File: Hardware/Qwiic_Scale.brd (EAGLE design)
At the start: 25.4 x 35.6 mm, 68 parts, among them J1 CAP, J2 Qwiic, J3 PTH, J4 Qwiic, J7 Spring Terminal, U1 NAU7802

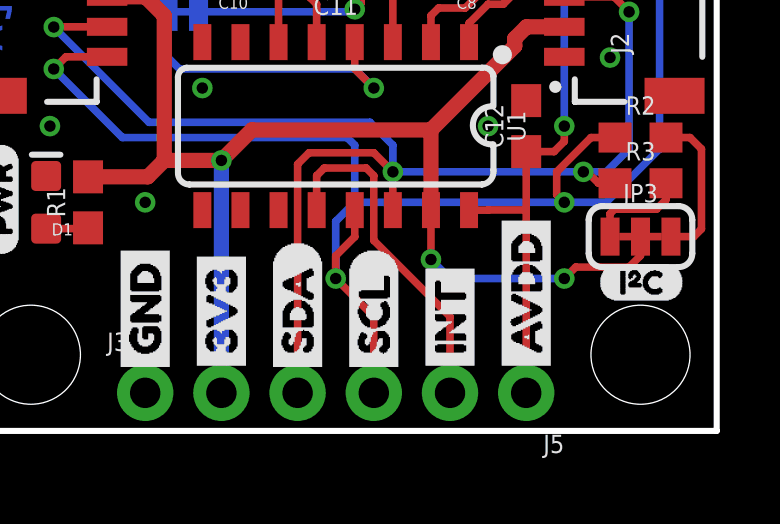
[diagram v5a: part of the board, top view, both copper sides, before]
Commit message: Change int flag to output
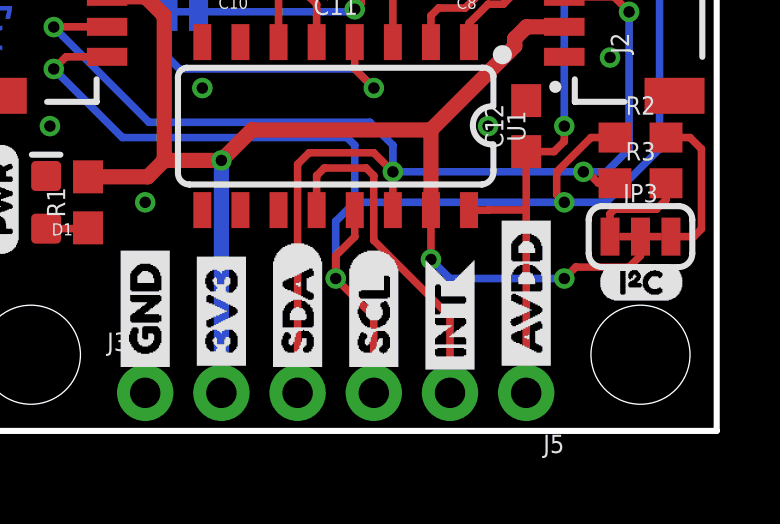
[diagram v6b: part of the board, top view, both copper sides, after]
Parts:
- removed U$16: (no value), buzzard_labels (5):INT8
- added U$21: (no value), buzzard_labels (62):INT0
- U$15: device buzzard_labels (5):INT8 -> buzzard_labels (62):INT0
- moved U$15 0.13 mm to (16.5, 1.52), flipped to the bottom
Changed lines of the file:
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@@
 <layer number="23" name="tOrigins" color="15" fill="1" visible="yes" active="yes"/>
 <layer number="24" name="bOrigins" color="15" fill="1" visible="yes" active="yes"/>
-<layer number="25" name="tNames" color="7" fill="1" visible="yes" active="yes"/>
-<layer number="26" name="bNames" color="7" fill="1" visible="yes" active="yes"/>
-<layer number="27" name="tValues" color="7" fill="1" visible="yes" active="yes"/>
-<layer number="28" name="bValues" color="7" fill="1" visible="yes" active="yes"/>
-<layer number="29" name="tStop" color="7" fill="3" visible="yes" active="yes"/>
-<layer number="30" name="bStop" color="7" fill="6" visible="yes" active="yes"/>
-<layer number="31" name="tCream" color="7" fill="4" visible="yes" active="yes"/>
-<layer number="32" name="bCream" color="7" fill="5" visible="yes" active="yes"/>
-<layer number="33" name="tFinish" color="6" fill="3" visible="yes" active="yes"/>
-<layer number="34" name="bFinish" color="6" fill="6" visible="yes" active="yes"/>
-<layer number="35" name="tGlue" color="7" fill="4" visible="yes" active="yes"/>
-<layer number="36" name="bGlue" color="7" fill="5" visible="yes" active="yes"/>
-<layer number="37" name="tTest" color="7" fill="1" visible="yes" active="yes"/>
-<layer number="38" name="bTest" color="7" fill="1" visible="yes" active="yes"/>
-<layer number="39" name="tKeepout" color="4" fill="11" visible="yes" active="yes"/>
-<layer number="40" name="bKeepout" color="1" fill="11" visible="yes" active="yes"/>
-<layer number="41" name="tRestrict" color="4" fill="10" visible="yes" active="yes"/>
-<layer number="42" name="bRestrict" color="1" fill="10" visible="yes" active="yes"/>
-<layer number="43" name="vRestrict" color="2" fill="10" visible="yes" active="yes"/>
-<layer number="44" name="Drills" color="7" fill="1" visible="yes" active="yes"/>
+<layer number="25" name="tNames" color="7" fill="1" visible="no" active="yes"/>
+<layer number="26" name="bNames" color="7" fill="1" visible="no" active="yes"/>
+<layer number="27" name="tValues" color="7" fill="1" visible="no" active="yes"/>
+<layer number="28" name="bValues" color="7" fill="1" visible="no" active="yes"/>
+<layer number="29" name="tStop" color="7" fill="3" visible="no" active="yes"/>
+<layer number="30" name="bStop" color="7" fill="6" visible="no" active="yes"/>
+<layer number="31" name="tCream" color="7" fill="4" visible="no" active="yes"/>
+<layer number="32" name="bCream" color="7" fill="5" visible="no" active="yes"/>
+<layer number="33" name="tFinish" color="6" fill="3" visible="no" active="yes"/>
+<layer number="34" name="bFinish" color="6" fill="6" visible="no" active="yes"/>
+<layer number="35" name="tGlue" color="7" fill="4" visible="no" active="yes"/>
+<layer number="36" name="bGlue" color="7" fill="5" visible="no" active="yes"/>
+<layer number="37" name="tTest" color="7" fill="1" visible="no" active="yes"/>
+<layer number="38" name="bTest" color="7" fill="1" visible="no" active="yes"/>
+<layer number="39" name="tKeepout" color="4" fill="11" visible="no" active="yes"/>
+<layer number="40" name="bKeepout" color="1" fill="11" visible="no" active="yes"/>
+<layer number="41" name="tRestrict" color="4" fill="10" visible="no" active="yes"/>
+<layer number="42" name="bRestrict" color="1" fill="10" visible="no" active="yes"/>
+<layer number="43" name="vRestrict" color="2" fill="10" visible="no" active="yes"/>
+<layer number="44" name="Drills" color="7" fill="1" visible="no" active="yes"/>
 <layer number="45" name="Holes" color="7" fill="1" visible="yes" active="yes"/>
-<layer number="46" name="Milling" color="3" fill="1" visible="yes" active="yes"/>
-<layer number="47" name="Measures" color="7" fill="1" visible="yes" active="yes"/>
-<layer number="48" name="Document" color="7" fill="1" visible="yes" active="yes"/>
-<layer number="49" name="Reference" color="7" fill="1" visible="yes" active="yes"/>
-<layer number="50" name="dxf" color="7" fill="1" visible="yes" active="yes"/>
+<layer number="46" name="Milling" color="3" fill="1" visible="no" active="yes"/>
+<layer number="47" name="Measures" color="7" fill="1" visible="no" active="yes"/>
+<layer number="48" name="Document" color="7" fill="1" visible="no" active="yes"/>
+<layer number="49" name="Reference" color="7" fill="1" visible="no" active="yes"/>
+<layer number="50" name="dxf" color="7" fill="1" visible="no" active="yes"/>
 <layer number="51" name="tDocu" color="6" fill="1" visible="yes" active="yes"/>
-<layer number="52" name="bDocu" color="7" fill="1" visible="yes" active="yes"/>
+<layer number="52" name="bDocu" color="7" fill="1" visible="no" active="yes"/>
 <layer number="91" name="Nets" color="2" fill="1" visible="no" active="no"/>
 <layer number="92" name="Busses" color="1" fill="1" visible="no" active="no"/>
@@
 <element name="U$8" library="Labels" package="GND-04" value="" x="6.35" y="1.651" smashed="yes" rot="R90"/>
 <element name="U$9" library="Labels" package="GND-04" value="" x="6.35" y="1.651" smashed="yes" rot="MR90"/>
-<element name="U$15" library="buzzard_labels (5)" package="INT8" value="" x="16.51" y="1.651" smashed="yes" rot="R90"/>
-<element name="U$16" library="buzzard_labels (5)" package="INT8" value="" x="16.51" y="1.651" smashed="yes" rot="MR90"/>
 <element name="D1" library="SparkFun-LED" package="LED-0603" value="RED" x="3.048" y="7.62" smashed="yes" rot="R90">
 <attribute name="NAME" x="3.937" y="6.9215" size="0.4064" layer="25" rot="R180"/>
@@
 <element name="U$14" library="buzzard_labels (68)" package="QWIIC2" value="" x="17.399" y="10.414" smashed="yes" rot="MR0"/>
 <element name="U$17" library="buzzard_labels (68)" package="SCALE3" value="" x="17.399" y="8.128" smashed="yes" rot="MR0"/>
+<element name="U$21" library="buzzard_labels (62)" package="INT0" value="" x="16.51" y="1.524" smashed="yes" rot="R90"/>
+<element name="U$15" library="buzzard_labels (62)" package="INT0" value="" x="16.51" y="1.524" smashed="yes" rot="MR90"/>
 </elements>
 <signals>

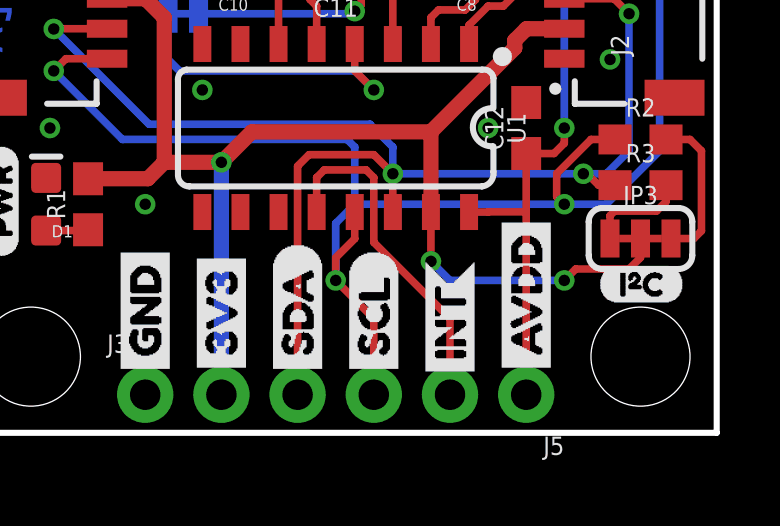
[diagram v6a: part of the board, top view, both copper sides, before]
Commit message: Changing int flag to output
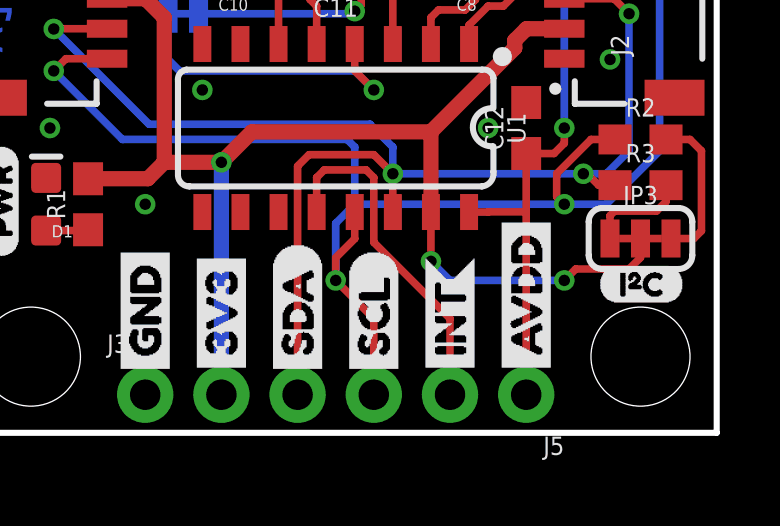
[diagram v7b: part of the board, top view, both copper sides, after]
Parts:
- moved U$15 0.13 mm to (16.5, 1.65)
- moved U$21 0.13 mm to (16.5, 1.65)
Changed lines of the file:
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@@
 <element name="U$14" library="buzzard_labels (68)" package="QWIIC2" value="" x="17.399" y="10.414" smashed="yes" rot="MR0"/>
 <element name="U$17" library="buzzard_labels (68)" package="SCALE3" value="" x="17.399" y="8.128" smashed="yes" rot="MR0"/>
-<element name="U$21" library="buzzard_labels (62)" package="INT0" value="" x="16.51" y="1.524" smashed="yes" rot="R90"/>
-<element name="U$15" library="buzzard_labels (62)" package="INT0" value="" x="16.51" y="1.524" smashed="yes" rot="MR90"/>
+<element name="U$21" library="buzzard_labels (62)" package="INT0" value="" x="16.51" y="1.651" smashed="yes" rot="R90"/>
+<element name="U$15" library="buzzard_labels (62)" package="INT0" value="" x="16.51" y="1.651" smashed="yes" rot="MR90"/>
 </elements>
 <signals>

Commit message: Remove extraneous wire from schematic
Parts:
- removed U$26: QWIIC_LOGO_8MM, Qwiic_Logo:QWIIC_8MM
- added U$16: QWIIC_LOGO_7MM, SparkFun-Aesthetics:QWIIC_7MM
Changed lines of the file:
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@@
 <layer number="44" name="Drills" color="7" fill="1" visible="no" active="yes"/>
 <layer number="45" name="Holes" color="7" fill="1" visible="yes" active="yes"/>
-<layer number="46" name="Milling" color="3" fill="1" visible="no" active="yes"/>
+<layer number="46" name="Milling" color="3" fill="1" visible="yes" active="yes"/>
 <layer number="47" name="Measures" color="7" fill="1" visible="no" active="yes"/>
 <layer number="48" name="Document" color="7" fill="1" visible="no" active="yes"/>
@@
 </element>
 <element name="U$20" library="buzzard_labels (15)" package="CAP0" value="" x="5.334" y="10.922" smashed="yes" rot="MR90"/>
-<element name="U$26" library="Qwiic_Logo" package="QWIIC_8MM" value="QWIIC_LOGO_8MM" x="18.161" y="25.781" smashed="yes" rot="MR90"/>
 <element name="U$14" library="buzzard_labels (68)" package="QWIIC2" value="" x="17.399" y="10.414" smashed="yes" rot="MR0"/>
 <element name="U$17" library="buzzard_labels (68)" package="SCALE3" value="" x="17.399" y="8.128" smashed="yes" rot="MR0"/>
 <element name="U$21" library="buzzard_labels (62)" package="INT0" value="" x="16.51" y="1.651" smashed="yes" rot="R90"/>
 <element name="U$15" library="buzzard_labels (62)" package="INT0" value="" x="16.51" y="1.651" smashed="yes" rot="MR90"/>
+<element name="U$16" library="SparkFun-Aesthetics" package="QWIIC_7MM" value="QWIIC_LOGO_7MM" x="17.78" y="25.4" smashed="yes" rot="MR90"/>
 </elements>
 <signals>
